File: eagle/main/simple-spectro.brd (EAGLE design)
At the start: 99.1 x 73.7 mm, 53 parts, among them CON1 BAT, CON2 SPI, CON3 SPI, CON4 VIBR, IC1 32U4, IC2 MCP73831T, IC3 MCP1703CB, IC4 DMP1045U, Q6 BSP75, U1 NCT75DMR2G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

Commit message: finalizing 1.6.0
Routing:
- net GND: track 99.9 -> 122.3 mm, vias 14 -> 16
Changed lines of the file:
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@@
 <wire x1="75.64714375" y1="61.595" x2="75.885" y2="61.595" width="0.4064" layer="16"/>
 <wire x1="75.885" y1="61.595" x2="76.2" y2="61.595" width="0.4064" layer="16"/>
-<wire x1="76.2" y1="61.595" x2="76.2" y2="63.4492" width="0" layer="19" extent="1-16"/>
-<wire x1="76.2" y1="63.4492" x2="76.2" y2="63.4492" width="0" layer="19" extent="1-16"/>
-<wire x1="74.2649" y1="66.04" x2="75.01214375" y2="66.04" width="0.4064" layer="16"/>
+<wire x1="75.01214375" y1="66.04" x2="74.2649" y2="66.04" width="0.4064" layer="16"/>
 <wire x1="75.01214375" y1="66.04" x2="75.64714375" y2="65.405" width="0.4064" layer="16"/>
 <wire x1="75.64714375" y1="65.405" x2="75.64714375" y2="61.595" width="0.4064" layer="16"/>
@@
 <wire x1="33.02" y1="10.16" x2="32.875" y2="10.015" width="0.4064" layer="16"/>
 <wire x1="32.875" y1="10.015" x2="32.725" y2="10.015" width="0.4064" layer="16"/>
-<wire x1="30.115" y1="6.35" x2="31.425" y2="10.015" width="0" layer="19" extent="16-16"/>
-<wire x1="30.115" y1="3.81" x2="30.115" y2="6.35" width="0" layer="19" extent="16-16"/>
-<wire x1="27.305" y1="14.097" x2="32.725" y2="14.115" width="0" layer="19" extent="16-16"/>
-<wire x1="18.974" y1="2.769" x2="30.115" y2="3.81" width="0" layer="19" extent="16-16"/>
+<wire x1="29.074" y1="2.769" x2="18.974" y2="2.769" width="0.4064" layer="16"/>
+<wire x1="29.074" y1="2.769" x2="30.115" y2="3.81" width="0.4064" layer="16"/>
+<wire x1="30.115" y1="6.35" x2="30.115" y2="3.81" width="0.4064" layer="16"/>
+<wire x1="32.075" y1="10.015" x2="32.075" y2="9.215" width="0.4064" layer="16"/>
+<wire x1="32.075" y1="9.215" x2="30.48" y2="7.62" width="0.4064" layer="16"/>
+<wire x1="30.48" y1="7.62" x2="30.48" y2="6.715" width="0.4064" layer="16"/>
+<wire x1="30.48" y1="6.715" x2="30.115" y2="6.35" width="0.4064" layer="16"/>
+<wire x1="27.94" y1="1.905" x2="27.94" y2="2.769" width="0.4064" layer="16"/>
+<via x="27.94" y="1.905" extent="1-16" drill="0.35"/>
+<wire x1="74.2649" y1="66.04" x2="72.39" y2="66.04" width="0.4064" layer="16"/>
+<via x="72.39" y="66.04" extent="1-16" drill="0.35"/>
+<wire x1="27.94" y1="2.769" x2="29.074" y2="2.769" width="0.4064" layer="16"/>
 </signal>
 <signal name="SCK">

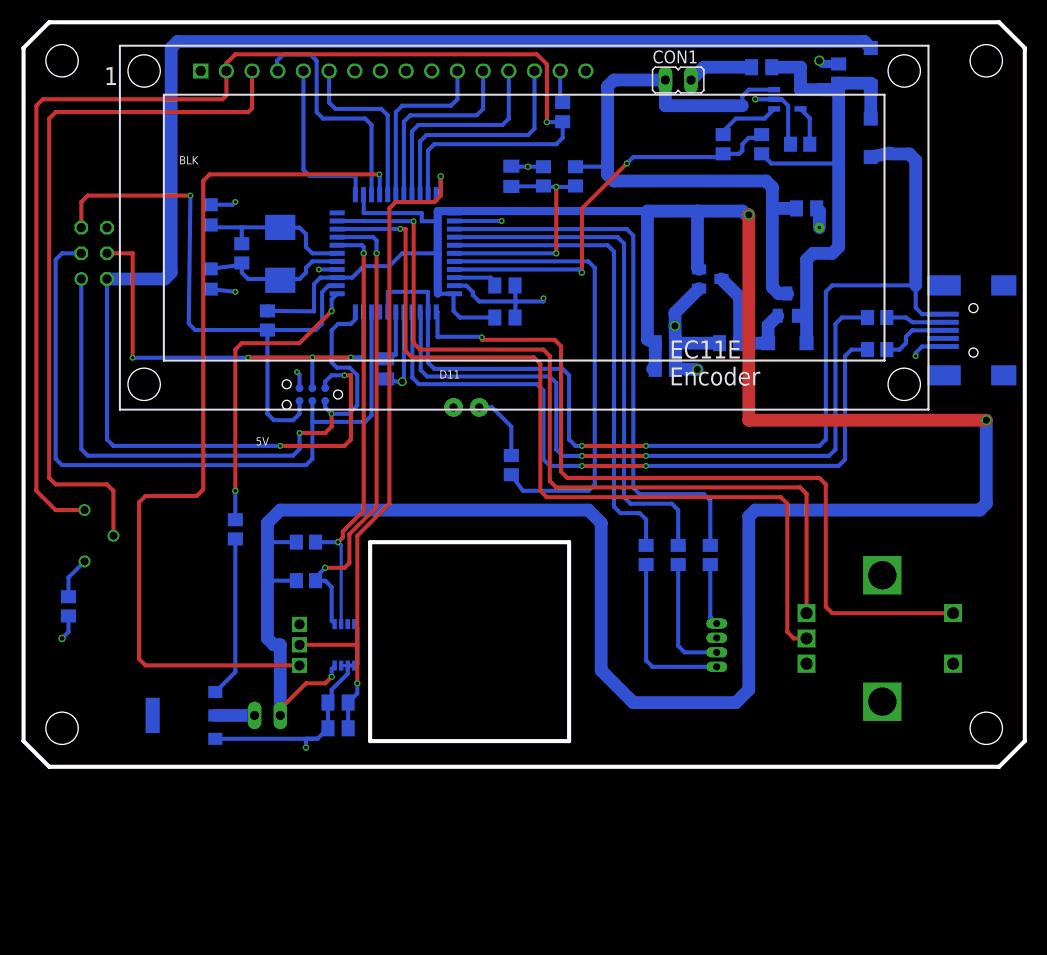
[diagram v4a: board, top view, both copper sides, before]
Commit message: add varistor to protect usb
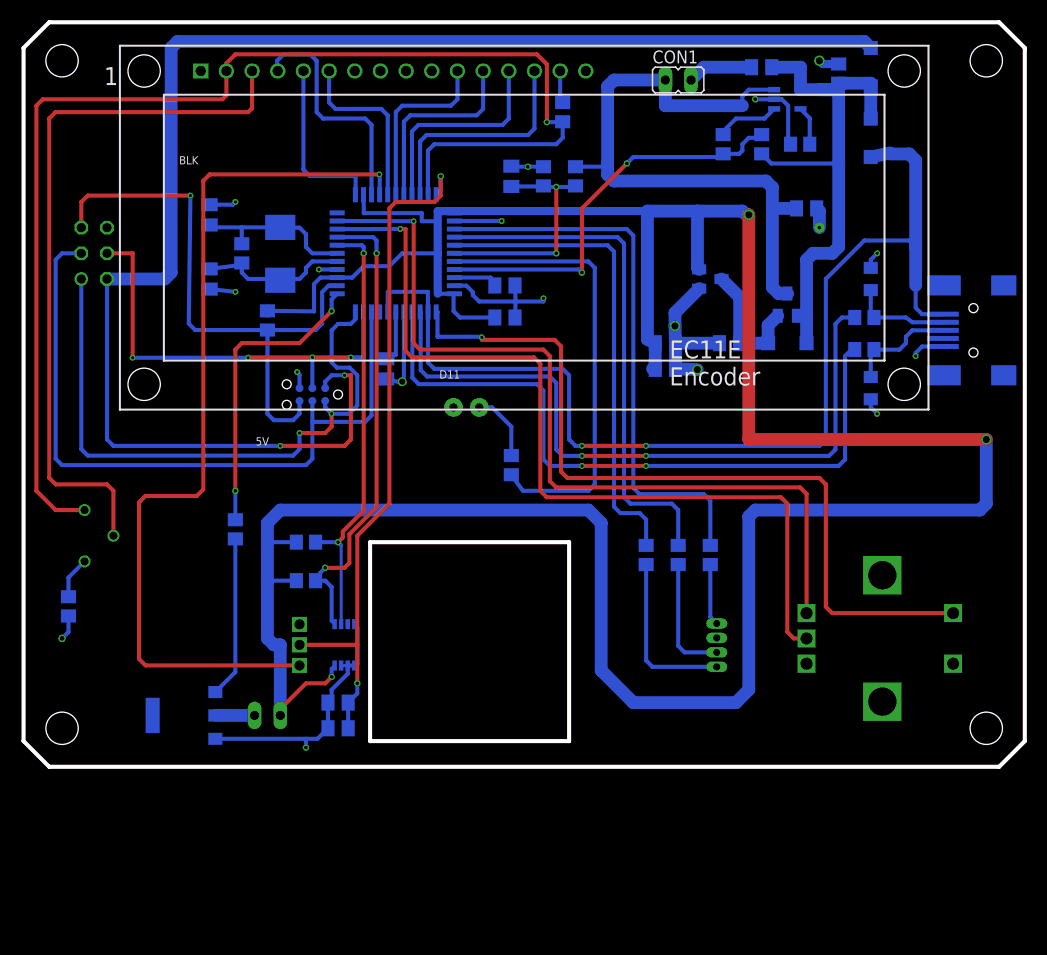
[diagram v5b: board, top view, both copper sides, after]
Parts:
- added Z1, Z2: VARISTOR, varistor:CT/CN0805
- moved R4 1.27 mm to (83.2, 41.3)
- moved R5 1.27 mm to (83.2, 44.5)
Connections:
- net GND: now also Z1.2, Z2.1
- net USBC_N: now also Z1.1
- net USBC_P: now also Z2.2
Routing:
- net USBC_P: track 6.74 -> 10.8 mm
- net USBC_N: track 5.73 -> 9.84 mm
- net VUSB: track 105.9 -> 108.8 mm
- net GND: track 122.3 -> 124.6 mm, vias 16 -> 18
- net USB_P: track 70.0 -> 68.7 mm
- net USB_N: track 70.3 -> 69.1 mm
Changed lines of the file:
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@@
 <attribute name="VALUE" x="98.425" y="36.195" size="1.27" layer="28" rot="MR0"/>
 </element>
-<element name="R4" library="rcl" package="R0805" value="22" x="84.455" y="41.275" smashed="yes" rot="MR180">
-<attribute name="ELECROW" value="C17561" x="84.455" y="41.275" size="1.778" layer="28" rot="MR180" display="off"/>
-<attribute name="LCSC" value="C17561" x="84.455" y="41.275" size="1.778" layer="28" rot="MR180" display="off"/>
-<attribute name="NAME" x="81.773109375" y="42.5091625" size="1.27" layer="26" rot="MR270"/>
-<attribute name="VALUE" x="83.297290625" y="39.7712875" size="1.27" layer="28" rot="MR180"/>
-</element>
-<element name="R5" library="rcl" library_urn="urn:adsk.eagle:library:334" package="R0805" package3d_urn="urn:adsk.eagle:package:23553/2" value="22" x="84.455" y="44.45" smashed="yes" rot="MR180">
-<attribute name="ELECROW" value="C17561" x="84.455" y="44.45" size="1.778" layer="28" rot="MR180" display="off"/>
-<attribute name="LCSC" value="C17561" x="84.455" y="44.45" size="1.778" layer="28" rot="MR180" display="off"/>
-<attribute name="NAME" x="87.235653125" y="45.11359375" size="1.27" layer="26" rot="MR180"/>
-<attribute name="VALUE" x="83.148409375" y="47.119859375" size="1.27" layer="28" rot="MR180"/>
+<element name="R4" library="rcl" package="R0805" value="22" x="83.185" y="41.275" smashed="yes" rot="MR180">
+<attribute name="ELECROW" value="C17561" x="83.185" y="41.275" size="1.778" layer="28" rot="MR180" display="off"/>
+<attribute name="LCSC" value="C17561" x="83.185" y="41.275" size="1.778" layer="28" rot="MR180" display="off"/>
+<attribute name="NAME" x="80.503109375" y="42.5091625" size="1.27" layer="26" rot="MR270"/>
+<attribute name="VALUE" x="82.027290625" y="39.7712875" size="1.27" layer="28" rot="MR180"/>
+</element>
+<element name="R5" library="rcl" library_urn="urn:adsk.eagle:library:334" package="R0805" package3d_urn="urn:adsk.eagle:package:23553/2" value="22" x="83.185" y="44.45" smashed="yes" rot="MR180">
+<attribute name="ELECROW" value="C17561" x="83.185" y="44.45" size="1.778" layer="28" rot="MR180" display="off"/>
+<attribute name="LCSC" value="C17561" x="83.185" y="44.45" size="1.778" layer="28" rot="MR180" display="off"/>
+<attribute name="NAME" x="85.965653125" y="45.11359375" size="1.27" layer="26" rot="MR180"/>
+<attribute name="VALUE" x="81.878409375" y="48.389859375" size="1.27" layer="28" rot="MR180"/>
 </element>
 <element name="C10" library="rcl" library_urn="urn:adsk.eagle:library:334" package="C0805K" package3d_urn="urn:adsk.eagle:package:23681/2" value="100nF" x="47.625" y="47.625" smashed="yes" rot="MR180">
@@
 <attribute name="ELECROW" value="C17513" x="69.215" y="61.595" size="1.778" layer="28" rot="MR90" display="off"/>
 <attribute name="LCSC" value="C17513" x="69.215" y="61.595" size="1.778" layer="28" rot="MR90" display="off"/>
+</element>
+<element name="Z1" library="varistor" library_urn="urn:adsk.eagle:library:410" package="CT/CN0805" package3d_urn="urn:adsk.eagle:package:30598/1" value="VARISTOR" x="83.82" y="48.26" rot="MR90">
+<attribute name="LCSC" value="C79709" x="83.82" y="48.26" size="1.778" layer="28" rot="MR90" display="off"/>
+</element>
+<element name="Z2" library="varistor" library_urn="urn:adsk.eagle:library:410" package="CT/CN0805" package3d_urn="urn:adsk.eagle:package:30598/1" value="VARISTOR" x="83.82" y="37.465" rot="MR90">
+<attribute name="LCSC" value="C79709" x="83.82" y="37.465" size="1.778" layer="28" rot="MR90" display="off"/>
 </element>
 </elements>
@@
 <wire x1="33.02" y1="10.16" x2="32.875" y2="10.015" width="0.4064" layer="16"/>
 <wire x1="32.875" y1="10.015" x2="32.725" y2="10.015" width="0.4064" layer="16"/>
-<wire x1="29.074" y1="2.769" x2="18.974" y2="2.769" width="0.4064" layer="16"/>
+<wire x1="27.94" y1="2.769" x2="18.974" y2="2.769" width="0.4064" layer="16"/>
 <wire x1="29.074" y1="2.769" x2="30.115" y2="3.81" width="0.4064" layer="16"/>
 <wire x1="30.115" y1="6.35" x2="30.115" y2="3.81" width="0.4064" layer="16"/>
@@
 <via x="72.39" y="66.04" extent="1-16" drill="0.35"/>
 <wire x1="27.94" y1="2.769" x2="29.074" y2="2.769" width="0.4064" layer="16"/>
+<contactref element="Z1" pad="2"/>
+<contactref element="Z2" pad="1"/>
+<wire x1="83.82" y1="49.36" x2="83.82" y2="50.165" width="0.4064" layer="16"/>
+<wire x1="83.82" y1="50.165" x2="84.455" y2="50.8" width="0.4064" layer="16"/>
+<via x="84.455" y="50.8" extent="1-16" drill="0.3048"/>
+<wire x1="83.82" y1="36.365" x2="83.82" y2="35.56" width="0.4064" layer="16"/>
+<wire x1="83.82" y1="35.56" x2="84.455" y2="34.925" width="0.4064" layer="16"/>
+<via x="84.455" y="34.925" extent="1-16" drill="0.3048"/>
 </signal>
 <signal name="SCK">
@@
 <wire x1="80.3275" y1="31.3944" x2="79.6925" y2="30.7594" width="0.4064" layer="16"/>
 <wire x1="79.6925" y1="30.7594" x2="61.5823" y2="30.7594" width="0.4064" layer="16"/>
-<wire x1="83.505" y1="44.45" x2="80.9625" y2="44.45" width="0.4064" layer="16"/>
+<wire x1="82.235" y1="44.45" x2="80.9625" y2="44.45" width="0.4064" layer="16"/>
 <wire x1="80.9625" y1="44.45" x2="80.3275" y2="43.815" width="0.4064" layer="16"/>
 <wire x1="55.245" y1="30.7594" x2="53.34" y2="30.7594" width="0.4064" layer="16"/>
@@
 <wire x1="61.5823" y1="31.75" x2="78.74" y2="31.75" width="0.4064" layer="16"/>
 <wire x1="78.74" y1="31.75" x2="79.375" y2="32.385" width="0.4064" layer="16"/>
-<wire x1="79.375" y1="32.385" x2="79.375" y2="46.99" width="0.4064" layer="16"/>
-<wire x1="79.375" y1="46.99" x2="80.01" y2="47.625" width="0.4064" layer="16"/>
-<wire x1="80.01" y1="47.625" x2="88.265" y2="47.625" width="0.4064" layer="16"/>
+<wire x1="79.375" y1="32.385" x2="79.375" y2="48.26" width="0.4064" layer="16"/>
 <wire x1="88.265" y1="47.625" x2="88.265" y2="45.415" width="0.4064" layer="16"/>
 <wire x1="88.265" y1="45.415" x2="88.9" y2="44.78" width="0.4064" layer="16"/>
 <wire x1="88.9" y1="44.78" x2="90.98" y2="44.78" width="0.4064" layer="16"/>
-<wire x1="88.265" y1="47.625" x2="88.265" y2="59.9948" width="1.27" layer="16"/>
+<wire x1="88.265" y1="51.435" x2="88.265" y2="47.625" width="1.27" layer="16"/>
+<wire x1="88.265" y1="51.435" x2="88.265" y2="59.9948" width="1.27" layer="16"/>
 <wire x1="88.265" y1="59.9948" x2="87.63" y2="60.6298" width="1.27" layer="16"/>
 <wire x1="87.63" y1="60.6298" x2="85.725" y2="60.6298" width="1.27" layer="16"/>
@@
 <wire x1="54.61" y1="31.75" x2="53.975" y2="32.385" width="0.4064" layer="16"/>
 <wire x1="83.82" y1="60.33" x2="85.725" y2="60.73" width="1.27" layer="16"/>
+<wire x1="87.63" y1="52.07" x2="88.265" y2="51.435" width="0.4064" layer="16"/>
+<wire x1="79.375" y1="48.26" x2="83.185" y2="52.07" width="0.4064" layer="16"/>
+<wire x1="83.185" y1="52.07" x2="87.63" y2="52.07" width="0.4064" layer="16"/>
 </signal>
 <signal name="D6">
@@
 <wire x1="90.98" y1="43.98" x2="87.9348" y2="43.98" width="0.4064" layer="16"/>
 <wire x1="87.9348" y1="43.98" x2="87.2998" y2="44.45" width="0.4064" layer="16"/>
-<wire x1="87.2998" y1="44.45" x2="85.405" y2="44.45" width="0.4064" layer="16"/>
+<wire x1="84.135" y1="44.45" x2="87.2998" y2="44.45" width="0.4064" layer="16"/>
+<contactref element="Z1" pad="1"/>
+<wire x1="83.82" y1="47.16" x2="83.82" y2="44.765" width="0.4064" layer="16"/>
+<wire x1="83.82" y1="44.765" x2="84.135" y2="44.45" width="0.4064" layer="16"/>
 </signal>
 <signal name="USBC_P">
@@
 <wire x1="87.2998" y1="42.545" x2="87.2998" y2="41.91" width="0.4064" layer="16"/>
 <wire x1="87.2998" y1="41.91" x2="86.6648" y2="41.275" width="0.4064" layer="16"/>
-<wire x1="86.6648" y1="41.275" x2="85.405" y2="41.275" width="0.4064" layer="16"/>
+<wire x1="86.6648" y1="41.275" x2="84.135" y2="41.275" width="0.4064" layer="16"/>
+<contactref element="Z2" pad="2"/>
+<wire x1="84.135" y1="41.275" x2="83.82" y2="40.96" width="0.4064" layer="16"/>
+<wire x1="83.82" y1="40.96" x2="83.82" y2="38.565" width="0.4064" layer="16"/>
 </signal>
 <signal name="A0">
@@
 <wire x1="71.755" y1="54.3433" x2="71.755" y2="54.61" width="1.27" layer="16"/>
 <via x="71.755" y="54.61" extent="1-16" drill="0.7" shape="square"/>
-<wire x1="71.755" y1="54.61" x2="71.755" y2="34.29" width="1.27" layer="1"/>
-<wire x1="71.755" y1="34.29" x2="95.25" y2="34.29" width="1.27" layer="1"/>
-<wire x1="95.25" y1="34.29" x2="95.25" y2="26.035" width="1.27" layer="16"/>
+<wire x1="71.755" y1="54.61" x2="71.755" y2="32.385" width="1.27" layer="1"/>
+<wire x1="71.755" y1="32.385" x2="95.25" y2="32.385" width="1.27" layer="1"/>
+<wire x1="95.25" y1="32.385" x2="95.25" y2="26.035" width="1.27" layer="16"/>
 <wire x1="95.25" y1="26.035" x2="94.615" y2="25.4" width="1.27" layer="16"/>
 <wire x1="94.615" y1="25.4" x2="72.39" y2="25.4" width="1.27" layer="16"/>
@@
 <wire x1="71.755" y1="24.765" x2="71.755" y2="7.62" width="1.27" layer="16"/>
 <wire x1="24.13" y1="45.085" x2="24.13" y2="45.1079" width="1.27" layer="16"/>
-<via x="95.25" y="34.29" extent="1-16" drill="0.7" shape="square"/>
+<via x="95.25" y="32.385" extent="1-16" drill="0.7" shape="square"/>
 <wire x1="71.755" y1="7.62" x2="70.485" y2="6.35" width="1.27" layer="16"/>
 <wire x1="70.485" y1="6.35" x2="60.325" y2="6.35" width="1.27" layer="16"/>
@@
 <wire x1="81.28" y1="30.4038" x2="81.28" y2="40.64" width="0.4064" layer="16"/>
 <wire x1="81.28" y1="40.64" x2="81.915" y2="41.275" width="0.4064" layer="16"/>
-<wire x1="81.915" y1="41.275" x2="83.505" y2="41.275" width="0.4064" layer="16"/>
+<wire x1="81.915" y1="41.275" x2="82.235" y2="41.275" width="0.4064" layer="16"/>
 <contactref element="R4" pad="1"/>
 <contactref element="IC1" pad="4"/>

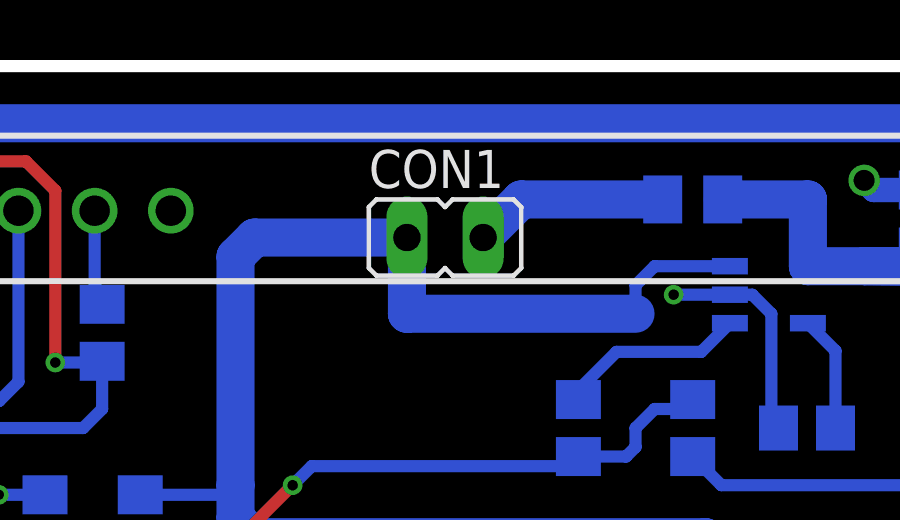
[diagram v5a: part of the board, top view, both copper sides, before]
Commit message: change side of battery connector and create gerber
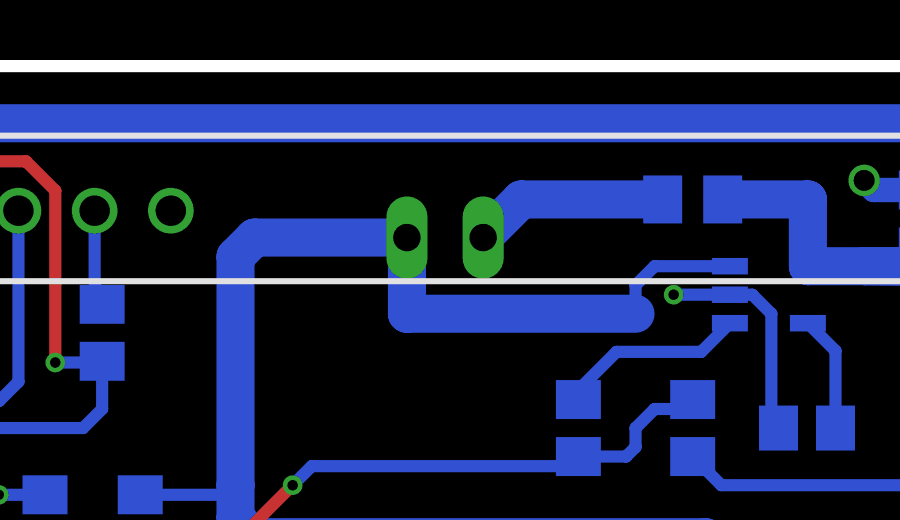
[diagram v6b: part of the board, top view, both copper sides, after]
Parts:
- flipped CON1 to the bottom, turned to 90 degrees
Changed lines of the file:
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@@
 </class>
 </classes>
-<designrules name="SeeedStudio_DRU_no_angle_20130527">
+<designrules name="SeeedStudio_DRU_no_angle_20130527 *">
 <description language="de">&lt;b&gt;EAGLE Design Rules&lt;/b&gt;
 &lt;p&gt;
@@
 <description language="zh">&lt;b&gt;Seeed Studio EAGLE Design Rules&lt;/b&gt;
 </description>
-<param name="layerSetup" value="(1*2*15*16)"/>
+<param name="layerSetup" value="(1*16)"/>
 <param name="mtCopper" value="0.035mm 0.0175mm 0.035mm 0.035mm 0.035mm 0.035mm 0.035mm 0.035mm 0.035mm 0.035mm 0.035mm 0.035mm 0.035mm 0.035mm 0.0175mm 0.035mm"/>
 <param name="mtIsolate" value="0.2mm 1.1mm 0.2mm 0.15mm 0.2mm 0.15mm 0.2mm 0.15mm 0.2mm 0.15mm 0.2mm 0.15mm 0.2mm 0.15mm 0.2mm"/>
@@
 </element>
 <element name="POT" library="dp_devices" package="TRIMMER_3362P" value="10k" x="6.35" y="22.86" rot="MR90"/>
-<element name="CON1" library="jumper" package="JP1" value="BAT" x="64.77" y="67.945" rot="R270"/>
+<element name="CON1" library="jumper" package="JP1" value="BAT" x="64.77" y="67.945" rot="MR90"/>
 <element name="U1" library="ti_tmp" package="MSOP8" value="NCT75DMR2G" x="31.75" y="12.065" smashed="yes" rot="MR180">
 <attribute name="LCSC" value="C94387" x="24.13" y="4.445" size="1.778" layer="28" rot="MR180" display="off"/>
